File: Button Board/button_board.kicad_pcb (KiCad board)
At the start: 2 copper layers, 46.2 x 24.6 mm, 16 parts, among them J1 Run_in+, J10 Reverse_in+, J11 brake+, J12 LED_Low_V+, J13 brake-, J14 running+, J15 running-, J2 Brake_in+, J3 Turn_in+, J4 turn+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

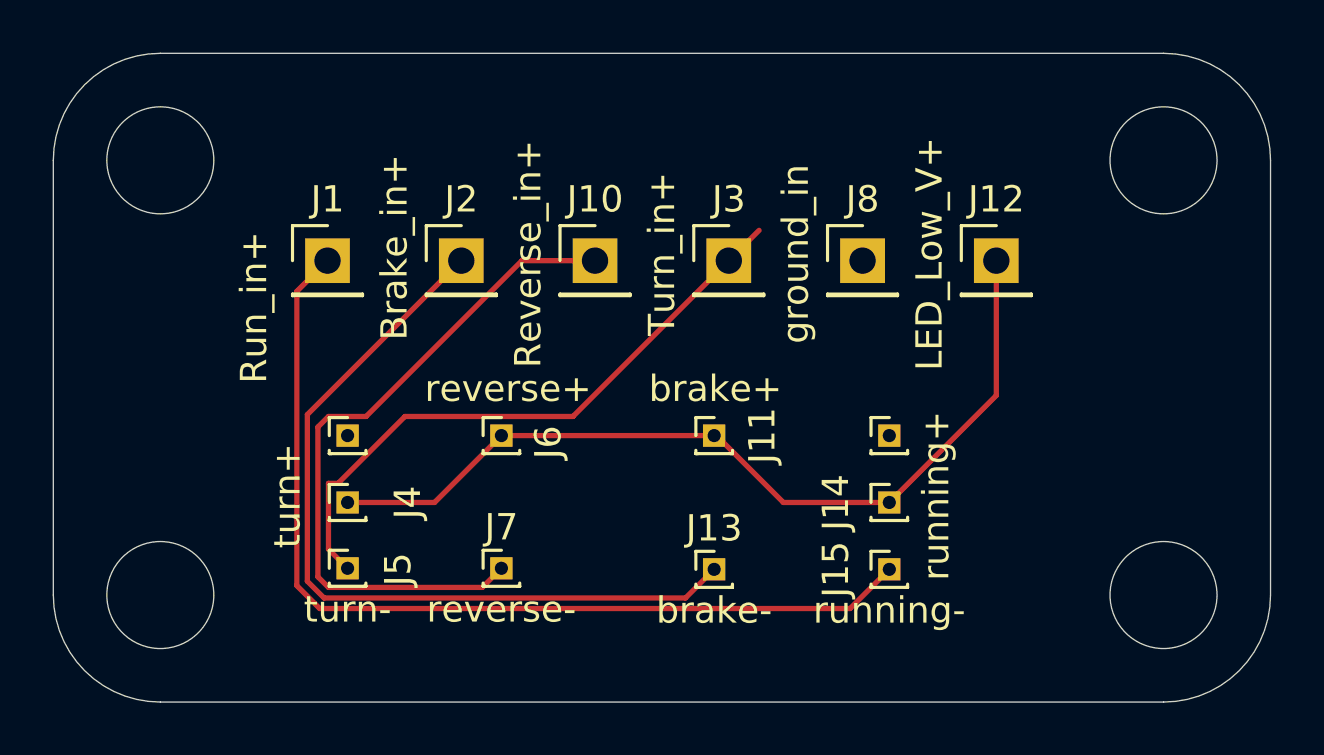
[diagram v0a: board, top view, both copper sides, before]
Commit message: LED Board, practice board, button board updates
Created led board and practice board/business card. Updated mounting for buttons on button board. Submitted all 3 for production on 4/6/25
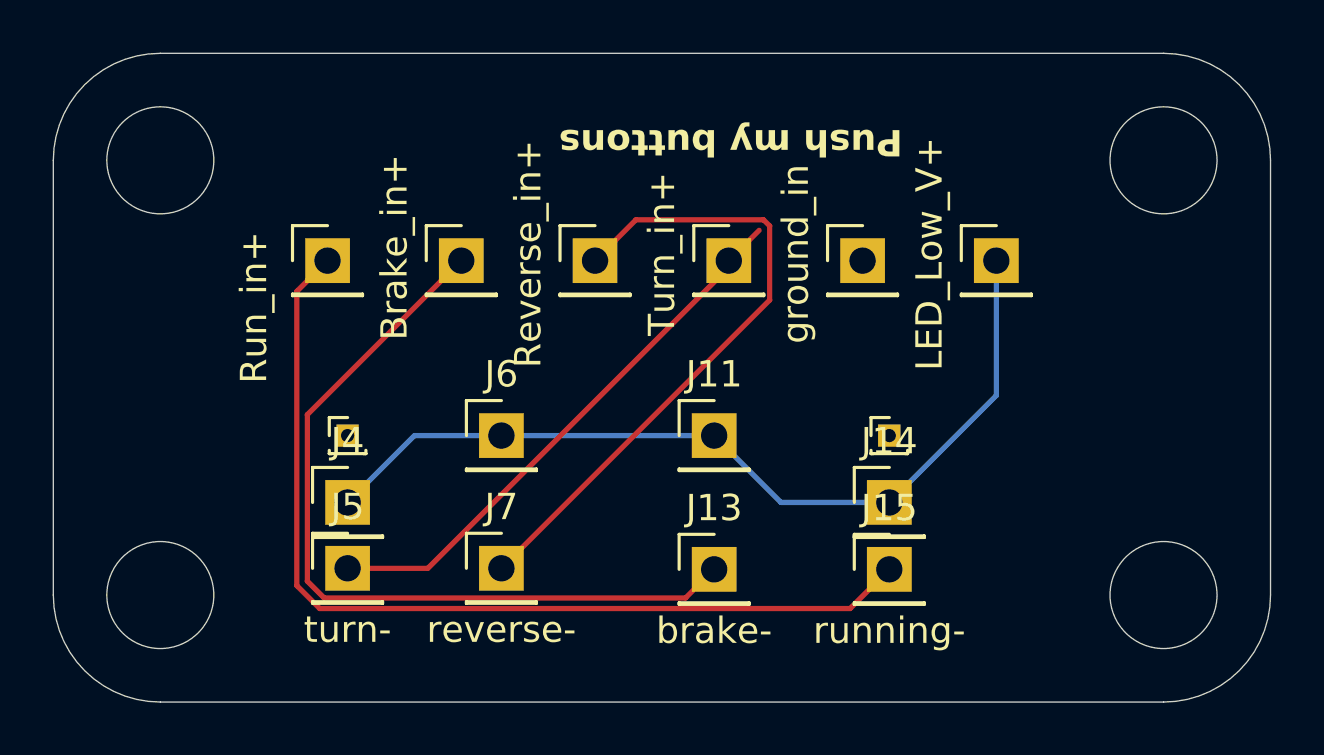
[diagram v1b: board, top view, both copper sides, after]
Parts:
- J11, J13, J14, J15, J4, J5, J6, J7: footprint Connector_PinHeader_1.00mm:PinHeader_1x01_P1.00mm_Vertical -> Connector_PinHeader_2.54mm:PinHeader_1x01_P2.54mm_Vertical
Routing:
- net Net-(J3-Pin_1): track 23.9 -> 22.1 mm
- net Net-(J10-Pin_1): track 26.3 -> 25.6 mm
